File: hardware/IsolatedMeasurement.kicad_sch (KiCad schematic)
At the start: 23 parts, among them IC12 UCC12040DVE, IC15 ISO6763FDWR, IC2 MCP3561T-E_NC, IC6 AP7365-33YRG-13, IC9 REF193GSZ-REEL, Q11 2N7002

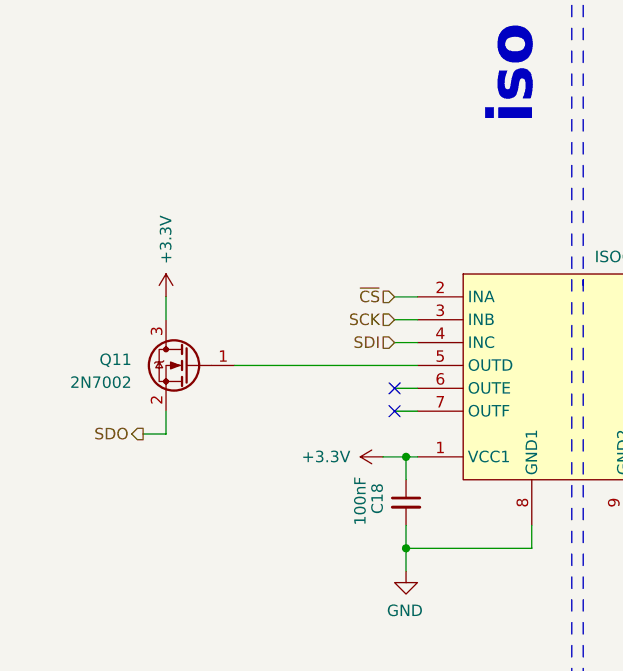
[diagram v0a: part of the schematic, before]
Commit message: moved hardware/main_board to hardware, deleted hardware/main_baord and hardware/connector_board, changed highside driveing transistors in acu and car HV mes to a open drain buffer for clarity and less ambiguous behavior
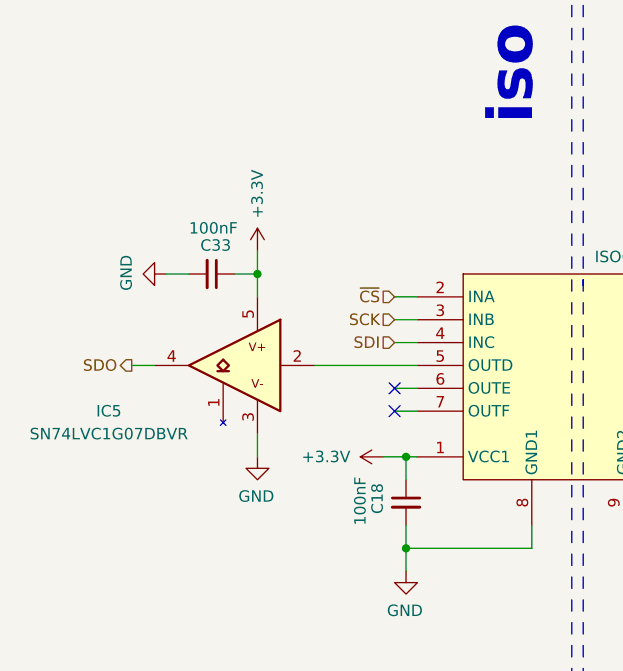
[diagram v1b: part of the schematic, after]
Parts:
- removed Q11: 2N7002, Package_TO_SOT_SMD:SOT-23, symbol Device:Q_NMOS_GSD
- added C33: 100nF, Capacitor_SMD:C_0603_1608Metric, symbol Device:C_Small
- added IC5: SN74LVC1G07DBVR, Package_TO_SOT_SMD:SOT-23-5, symbol Samacsys_kicad_sym:SN74LVC1G07DBVR
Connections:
- net +3V3: now also C33.1, IC5.5
- net GND: now also C33.2, IC5.3
- net SDO: now also IC5.4
- net at IC15.5 (OUTD): now also IC5.2

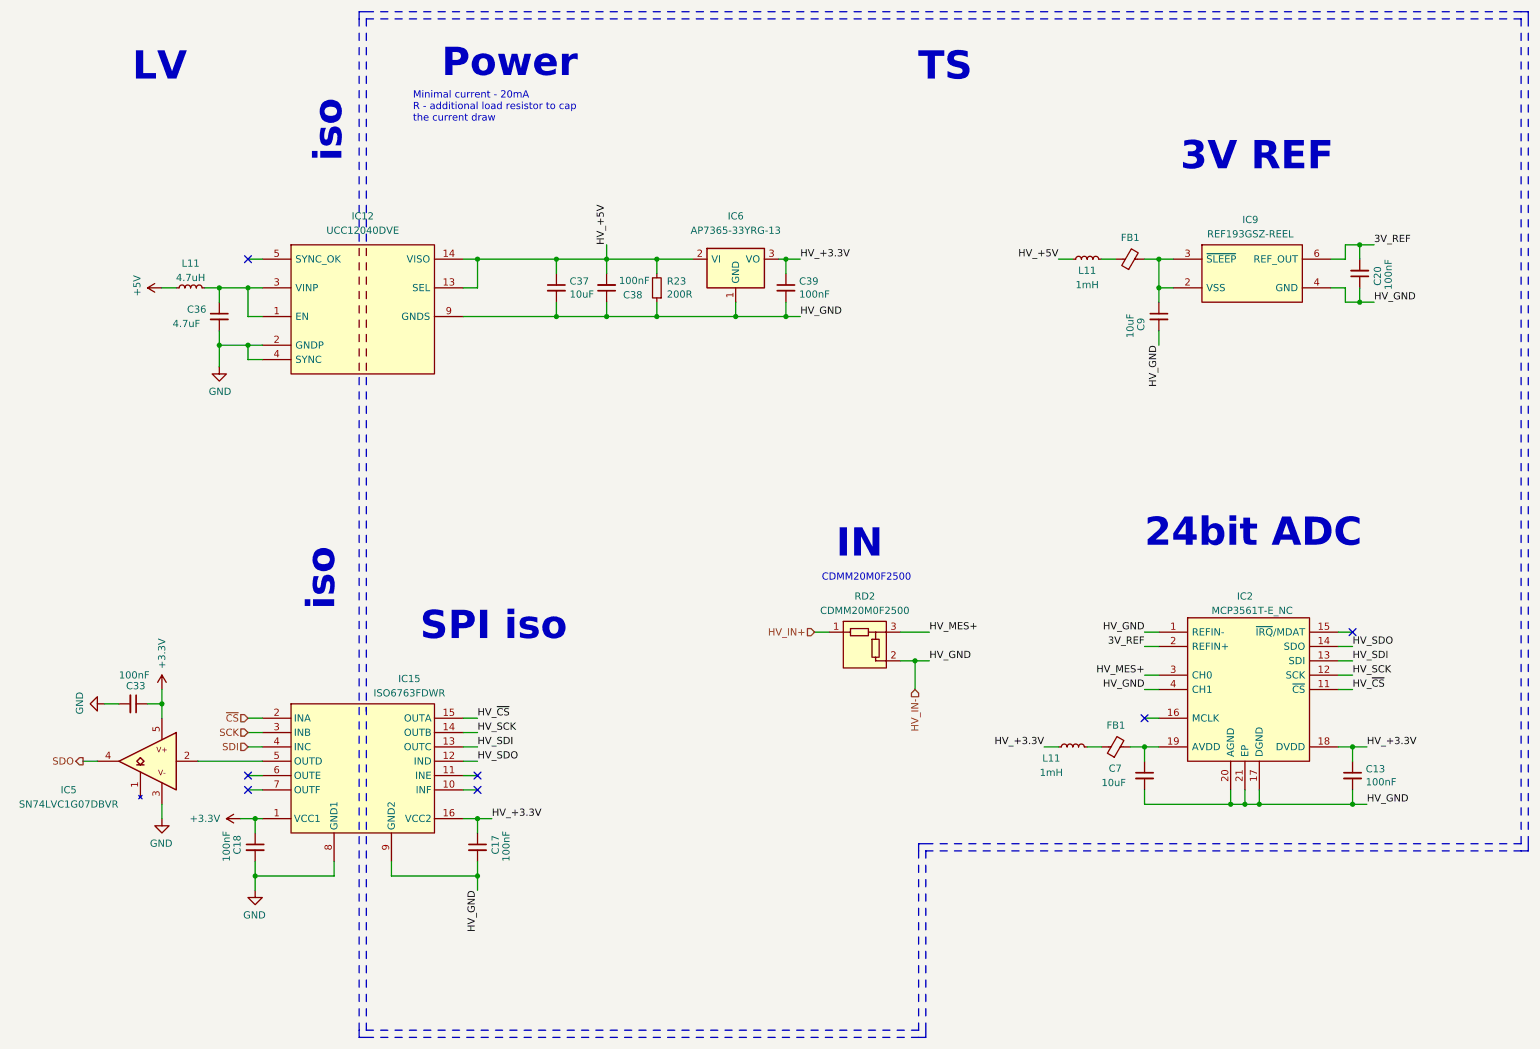
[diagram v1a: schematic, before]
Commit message: symbol update
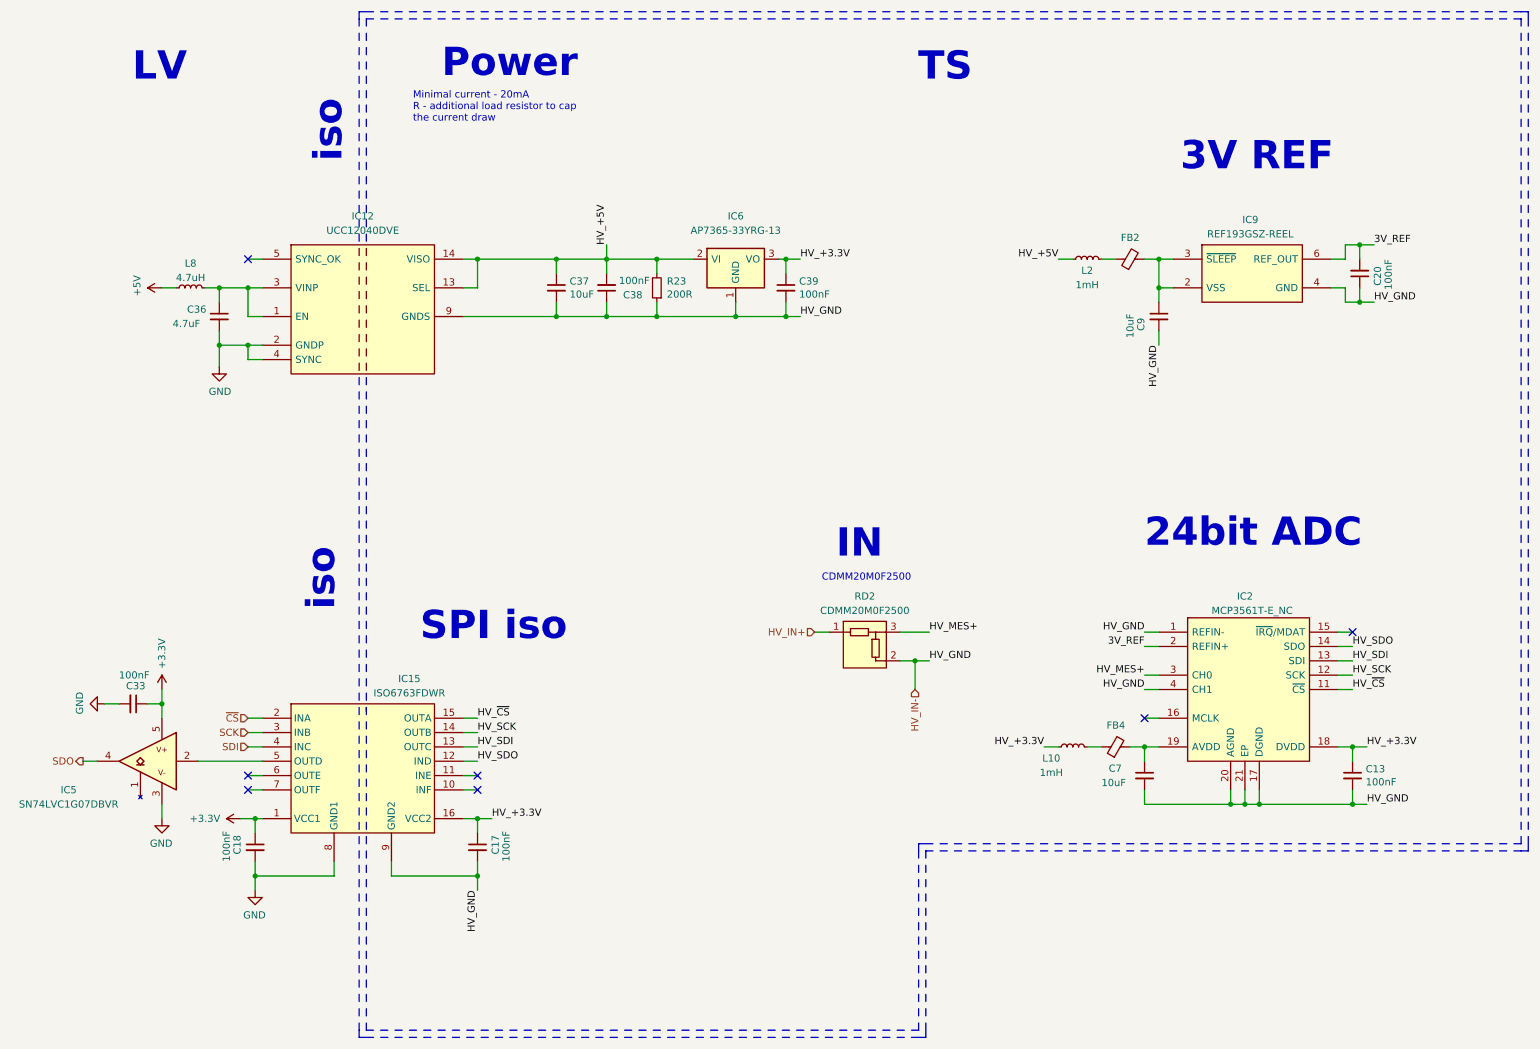
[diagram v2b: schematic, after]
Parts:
- renumbered FB1 to FB2, FB1 to FB4, L11 to L10, L11 to L2, L11 to L8
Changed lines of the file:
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@@
   (symbol (lib_id "Device:L_Small") (at 204.47 58.42 90) (unit 1)
     (in_bom yes) (on_board yes) (dnp no)
-    (property "Reference" "L11" (at 204.47 59.69 90)
+    (property "Reference" "L2" (at 204.47 59.69 90)
       (effects (font (size 1.27 1.27)) (justify bottom))
     )
@@
     (instances
       (project "PUTM_EV_BMS_HV_Master_2021"
-        (path "/b456cffc-d9d7-4c91-91f2-36ec9a65dd1b/66c3869d-de11-4d8d-b4de-9d98c32ec205"
-          (reference "L11") (unit 1)
-        )
         (path "/b456cffc-d9d7-4c91-91f2-36ec9a65dd1b/e61cc821-5479-4c04-b5ab-4a32f17b4f03/d2e30d51-b8f8-4bbd-bb5a-76e0eb119260"
           (reference "L2") (unit 1)
@@
   (symbol (lib_id "Device:Ferrite_Bead_Small") (at 212.09 58.42 90) (unit 1)
     (in_bom yes) (on_board yes) (dnp no)
-    (property "Reference" "FB1" (at 212.09 54.61 90)
+    (property "Reference" "FB2" (at 212.09 54.61 90)
       (effects (font (size 1.27 1.27)))
     )
@@
     (instances
       (project "PUTM_EV_BMS_HV_Master_2021"
-        (path "/b456cffc-d9d7-4c91-91f2-36ec9a65dd1b/66c3869d-de11-4d8d-b4de-9d98c32ec205"
-          (reference "FB1") (unit 1)
-        )
         (path "/b456cffc-d9d7-4c91-91f2-36ec9a65dd1b/e61cc821-5479-4c04-b5ab-4a32f17b4f03/d2e30d51-b8f8-4bbd-bb5a-76e0eb119260"
           (reference "FB2") (unit 1)
@@
   (symbol (lib_id "Device:Ferrite_Bead_Small") (at 209.55 144.78 90) (unit 1)
     (in_bom yes) (on_board yes) (dnp no)
-    (property "Reference" "FB1" (at 209.55 140.97 90)
+    (property "Reference" "FB4" (at 209.55 140.97 90)
       (effects (font (size 1.27 1.27)))
     )
@@
     (instances
       (project "PUTM_EV_BMS_HV_Master_2021"
-        (path "/b456cffc-d9d7-4c91-91f2-36ec9a65dd1b/66c3869d-de11-4d8d-b4de-9d98c32ec205"
-          (reference "FB1") (unit 1)
-        )
         (path "/b456cffc-d9d7-4c91-91f2-36ec9a65dd1b/e61cc821-5479-4c04-b5ab-4a32f17b4f03/d2e30d51-b8f8-4bbd-bb5a-76e0eb119260"
           (reference "FB4") (unit 1)
@@
   (symbol (lib_id "Device:L_Small") (at 201.93 144.78 90) (unit 1)
     (in_bom yes) (on_board yes) (dnp no)
-    (property "Reference" "L11" (at 198.12 146.05 90)
+    (property "Reference" "L10" (at 198.12 146.05 90)
       (effects (font (size 1.27 1.27)) (justify bottom))
     )
@@
     (instances
       (project "PUTM_EV_BMS_HV_Master_2021"
-        (path "/b456cffc-d9d7-4c91-91f2-36ec9a65dd1b/66c3869d-de11-4d8d-b4de-9d98c32ec205"
-          (reference "L11") (unit 1)
-        )
         (path "/b456cffc-d9d7-4c91-91f2-36ec9a65dd1b/e61cc821-5479-4c04-b5ab-4a32f17b4f03/d2e30d51-b8f8-4bbd-bb5a-76e0eb119260"
           (reference "L10") (unit 1)
@@
   (symbol (lib_id "Device:L_Small") (at 45.72 63.5 90) (unit 1)
     (in_bom yes) (on_board yes) (dnp no)
-    (property "Reference" "L11" (at 45.72 58.42 90)
+    (property "Reference" "L8" (at 45.72 58.42 90)
       (effects (font (size 1.27 1.27)) (justify bottom))
     )
@@
     (instances
       (project "PUTM_EV_BMS_HV_Master_2021"
-        (path "/b456cffc-d9d7-4c91-91f2-36ec9a65dd1b/66c3869d-de11-4d8d-b4de-9d98c32ec205"
-          (reference "L11") (unit 1)
-        )
         (path "/b456cffc-d9d7-4c91-91f2-36ec9a65dd1b/e61cc821-5479-4c04-b5ab-4a32f17b4f03/d2e30d51-b8f8-4bbd-bb5a-76e0eb119260"
           (reference "L8") (unit 1)

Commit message: schematic clean up
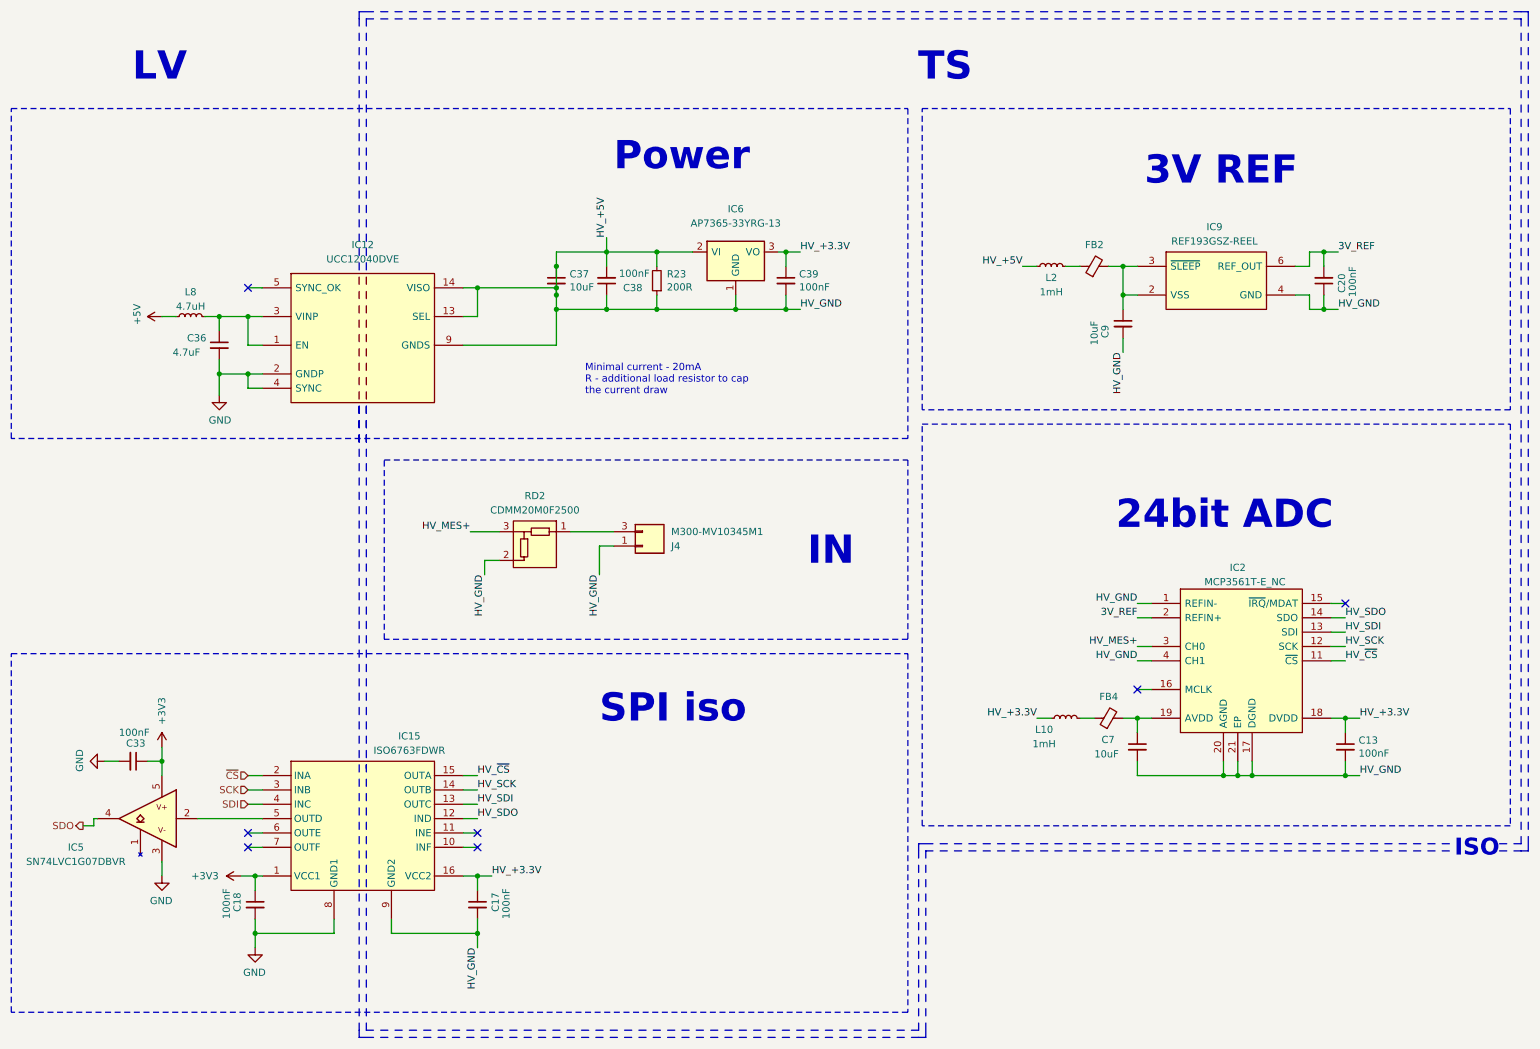
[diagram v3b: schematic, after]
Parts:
- added J4: M300-MV10345M1, M300MV10345M1, symbol M300-MV10345M1:M300-MV10345M1
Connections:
- net HV_IN- is gone; now on net HV_+5V: C13.2, C17.2, C20.1, C37.2, C38.1, C39.2, C7.2, C9.2, IC12.10 (NCS), IC12.11 (NCS), IC12.12 (NCS), IC12.15 (GNDS), IC12.16 (GNDS), IC12.9 (GNDS), IC15.9 (GND2), IC2.1 (REFIN-), IC2.17 (DGND), IC2.20 (AGND), IC2.21 (EP), IC2.4 (CH1), IC6.1 (GND), IC9.4 (GND), R23.1, RD2.2
- net HV_+5V: now also J4.1
- net HV_IN+: no longer names the net of RD2.1
- net HV_IN+: now also J4.3
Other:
- note added: "ISO"
- note removed: "CDMM20M0F2500"
- note removed: "iso"
- moved on the sheet: C13, C17, C18, C20, C33, C36, C37, C38, C39, C7, C9, FB2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

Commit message: relay new driving logic, some ltc communication changes
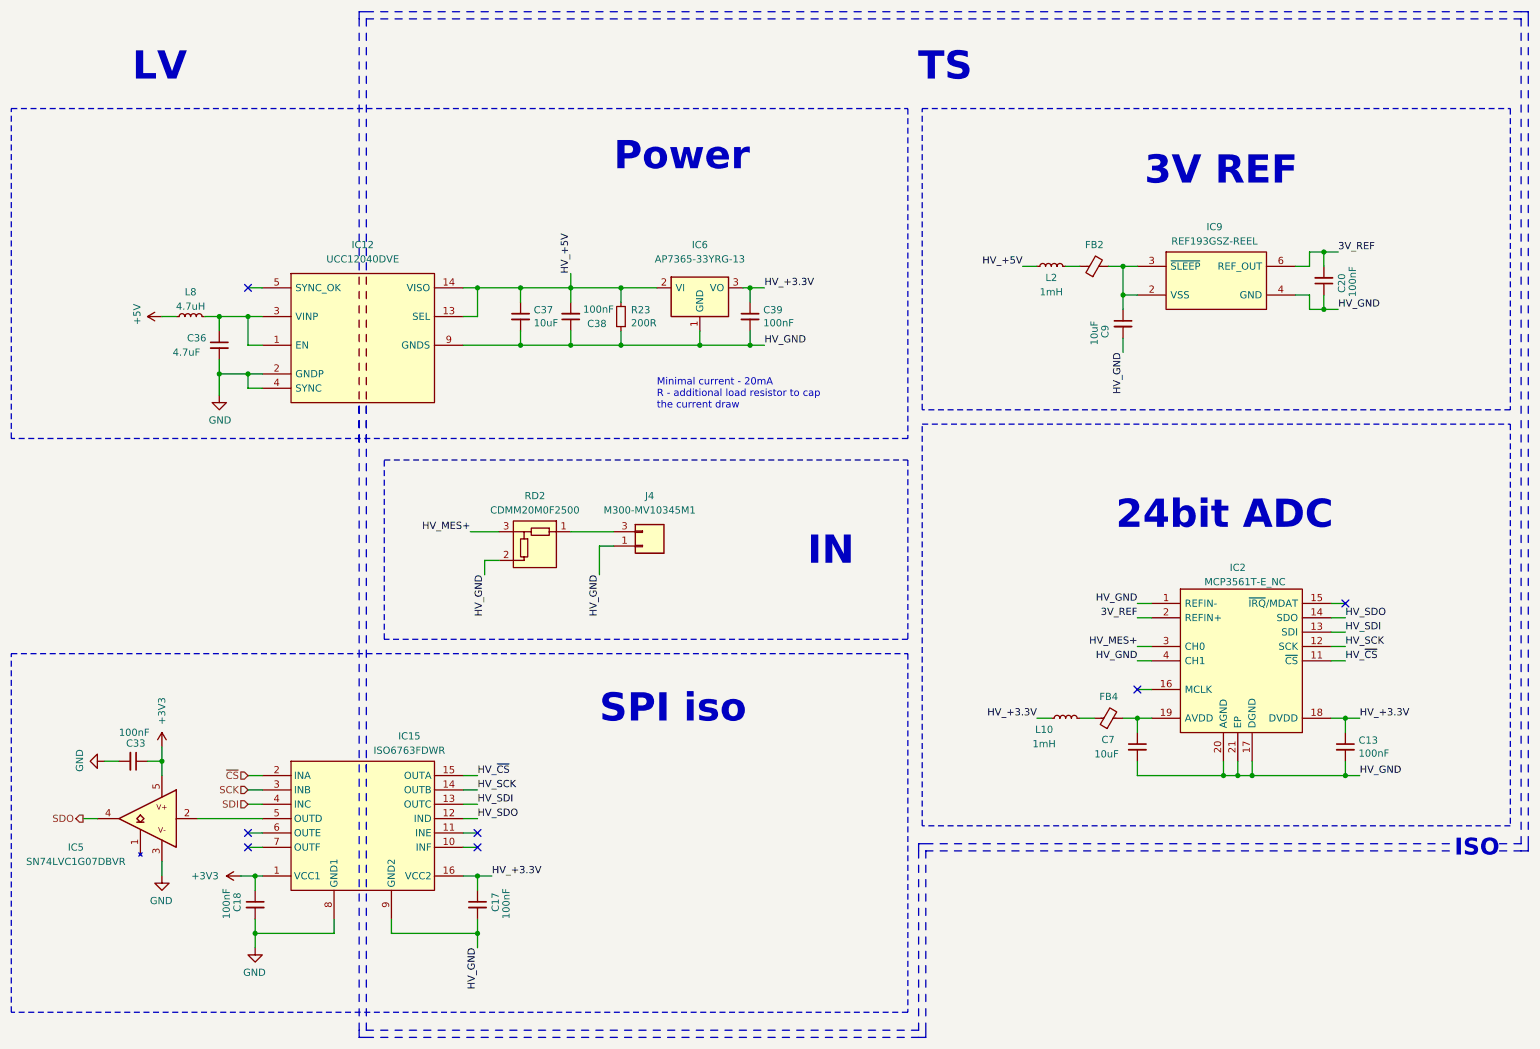
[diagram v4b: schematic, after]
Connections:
- net HV_+5V: no longer C13.2, C17.2, C20.1, C37.2, C38.1, C39.2, C7.2, C9.2, IC12.10 (NCS), IC12.11 (NCS), IC12.12 (NCS), IC12.15 (GNDS), IC12.16 (GNDS), IC12.9 (GNDS), IC15.9 (GND2), IC2.1 (REFIN-), IC2.17 (DGND), IC2.20 (AGND), IC2.21 (EP), IC2.4 (CH1), IC6.1 (GND), IC9.4 (GND), J4.1, R23.1, RD2.2
- new net HV_GND: C13.2, C17.2, C20.1, C37.2, C38.1, C39.2, C7.2, C9.2, IC12.10 (NCS), IC12.11 (NCS), IC12.12 (NCS), IC12.15 (GNDS), IC12.16 (GNDS), IC12.9 (GNDS), IC15.9 (GND2), IC2.1 (REFIN-), IC2.17 (DGND), IC2.20 (AGND), IC2.21 (EP), IC2.4 (CH1), IC6.1 (GND), IC9.4 (GND), J4.1, R23.1, RD2.2
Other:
- moved on the sheet: C37, C38, C39, IC6, R23
